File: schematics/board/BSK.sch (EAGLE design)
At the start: 58 parts, among them IC2 MAX809REUR, J1 idc_2x5, SW1 RST

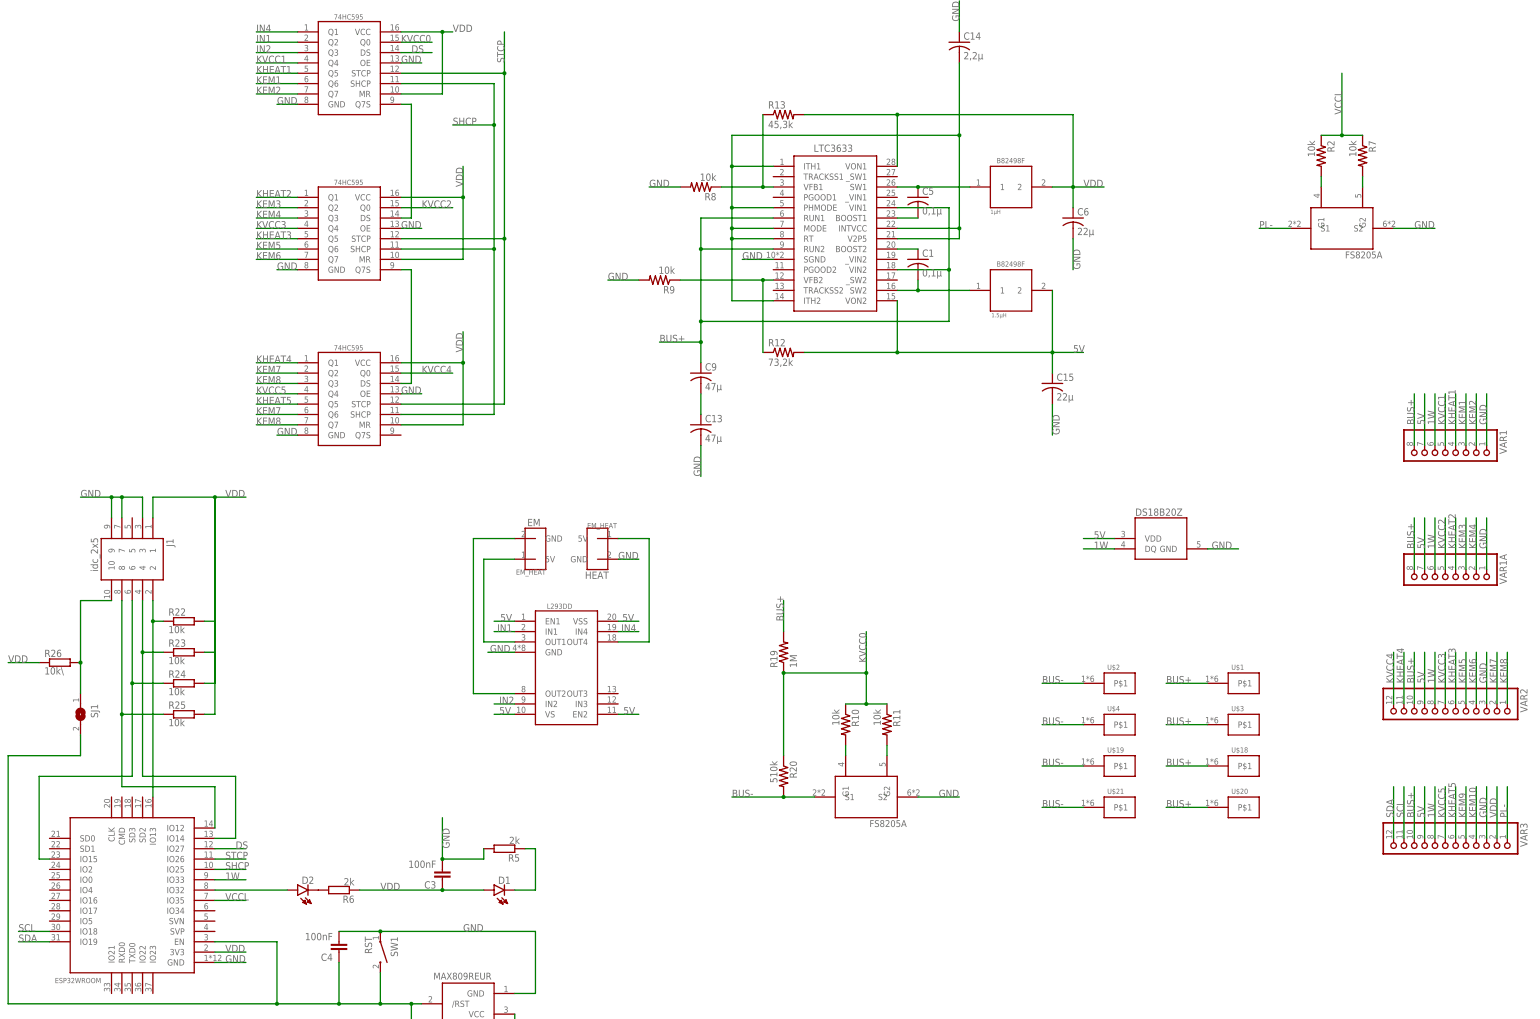
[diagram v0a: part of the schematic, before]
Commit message: изменен БСК4
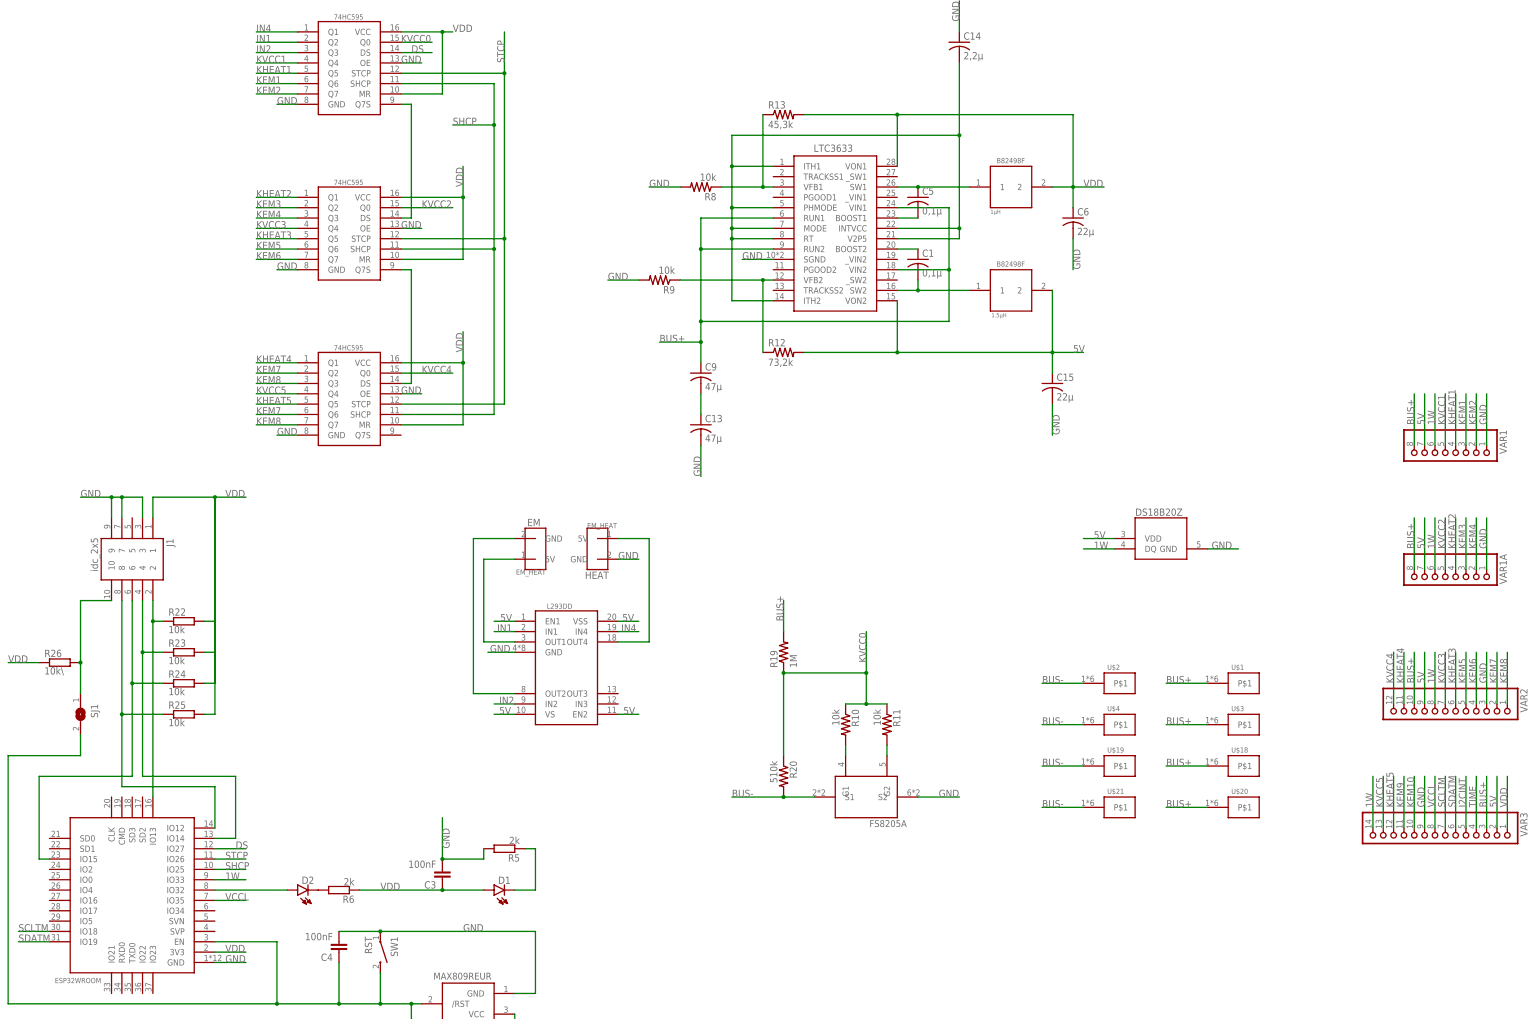
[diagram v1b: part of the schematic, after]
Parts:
- removed R2, R7: 10k, resistor:R-US_R0603
- removed U$16: FS8205A, CanCubeSat:FS8205A
- VAR3: device pinheadCS:PINHD-1X12 -> pinheadCS:PINHD-1X14
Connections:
- removed net N$4: R2.2, U$16.G1
- removed net N$6: R7.2, U$16.G2
- removed net PL-: U$16.S1, VAR3.1
- removed net SCL: U$13.IO18, VAR3.11
- removed net SDA: U$13.IO19, VAR3.12
- new net I2CINT: VAR3.5
- new net SCLTM: U$13.IO18, VAR3.7
- new net SDATM: U$13.IO19, VAR3.6
- new net TIME: VAR3.4
- net 1W: now also VAR3.14; no longer VAR3.8
- net 5V: now also VAR3.2; no longer VAR3.9
- net BUS+: now also VAR3.3; no longer VAR3.10
- net GND: now also VAR3.9; no longer U$16.S2, VAR3.3
- net KEM10: now also VAR3.10; no longer VAR3.4
- net KEM9: now also VAR3.11; no longer VAR3.5
- net KHEAT5: now also VAR3.12; no longer VAR3.6
- net KVCC5: now also VAR3.13; no longer VAR3.7
- net VCCL: now also VAR3.8; no longer R2.1, R7.1
- net VDD: now also VAR3.1; no longer VAR3.2

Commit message: изменен БСК1
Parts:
- removed C3, C4: 100nF, rcl:C-EUC0603
- removed D1, D2: HLMP6, display-hp:HLMP6
- removed IC2: MAX809REUR, MAX809_:MAX809EUR
- removed J1: idc_2x5, idc_2x5:3221-10-0100-00
- removed R21, R22, R23, R24, R25: 10k, resistor-shunt:BVS
- removed R26: 10k\, resistor-shunt:BVS
- removed R5, R6: 2k, resistor-shunt:BVS
- removed SW1: RST, 1437566-3:1437566-3
- added C2, C7: 10µ, rcl:C-USC0603
- added C33: 0,1µ, rcl:C-USC0603
- added R1: 510k, resistor:R-US_R0603
- added U$16: USB-C, CanCubeSat:USB-C
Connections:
- removed net N$17: D1.K, R5.2
- removed net N$18: D2.K, R6.1
- removed net N$21: C4.1, IC2./RST, R21.2, SJ1.2, SW1.2, U$13.EN
- removed net N$23: J1.4, R23.2, U$13.IO14
- removed net N$26: J1.8, R25.2, U$13.IO12
- removed net N$27: J1.6, R24.2, U$13.IO15
- removed net N$29: J1.10, R26.1, SJ1.1
- removed net VDD3: D2.A, U$13.IO32
- new net N$44: U$16.GND
- new net N$45: U$16.TX+
- new net N$46: U$16.VBUS
- new net N$47: U$16.RX+
- new net N$48: U$16.RES
- new net N$49: U$16.SWC
- new net N$50: U$16.SWD
- new net N$55: SJ1.2, U$13.IO0
- net GND: now also C2.2, C33.2, C7.2, SJ1.1; no longer C3.2, C4.2, IC2.GND, J1.3, J1.7, J1.9, R5.1, SW1.1
- net N$22: now also C7.1, R1.2, U$13.EN; no longer J1.2, R22.2, U$13.IO13
- net VDD: now also C2.1, C33.1, R1.1; no longer C3.1, D1.A, IC2.VCC, J1.1, R21.1, R22.1, R23.1, R24.1, R25.1, R26.2, R6.2
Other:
- moved on the sheet: SJ1

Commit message: доработана схема БСК1
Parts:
- removed SJ1: (no value), jumper:SJW
- removed U$14: FS8205A, CanCubeSat:FS8205A
- added R2: 5k, resistor:R-US_R0603
- added U$22: FS8205A+, CanCubeSat:FS8205A+
- C7: value 10µ -> 1nF
- R1: value 510k -> 12k
- U$5: value DS18B20ZDS18B20Z -> DS18B20Z; device CanCubeSat:DS18B20ZDS18B20Z -> CanCubeSat:DS18B20Z
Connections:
- removed net N$22: C7.1, R1.2, U$13.EN
- removed net N$44: U$16.GND
- removed net N$45: U$16.TX+
- removed net N$46: U$16.VBUS
- removed net N$47: U$16.RX+
- removed net N$48: U$16.RES
- removed net N$49: U$16.SWC
- removed net N$50: U$16.SWD
- removed net N$55: SJ1.2, U$13.IO0
- new net BUS+1: U$1.P$1
- new net BUS+2: U$18.P$1
- new net BUS+3: U$20.P$1
- new net BUS-1: U$4.P$1
- new net BUS-2: U$19.P$1
- new net BUS-3: U$21.P$1
- new net EN: C7.1, R1.1, U$13.EN, U$16.RES/EN
- new net HEAT: U$10.HEAT, U$13.HEAT, U$22.HEAT, U$5.HEAT, U$8.HEAT
- new net IO0: R2.1, U$13.IO0, U$16.IO0
- new net RX-C: U$13.RXD0, U$16.SWD/RXD
- new net TX-C: U$13.TXD0, U$16.SWC/TXD
- net BUS+: now also U$16.NC/VBUS; no longer U$1.P$1, U$18.P$1, U$20.P$1
- net BUS-: now also U$22.S1; no longer U$14.S1, U$19.P$1, U$21.P$1, U$4.P$1
- net GND: now also U$16.GND, U$22.S2; no longer SJ1.1, U$14.S2
- net KEM10: now also U$17.Q7
- net KEM7: no longer U$17.Q6
- net KEM8: no longer U$17.Q7
- net KEM9: now also U$17.Q6
- net N$8: now also U$22.G1; no longer U$14.G1
- net N$9: now also U$22.G2; no longer U$14.G2
- net VDD: now also R1.2, R2.2; no longer R1.1
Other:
- moved on the sheet: C1, C14, C5, C7, R1

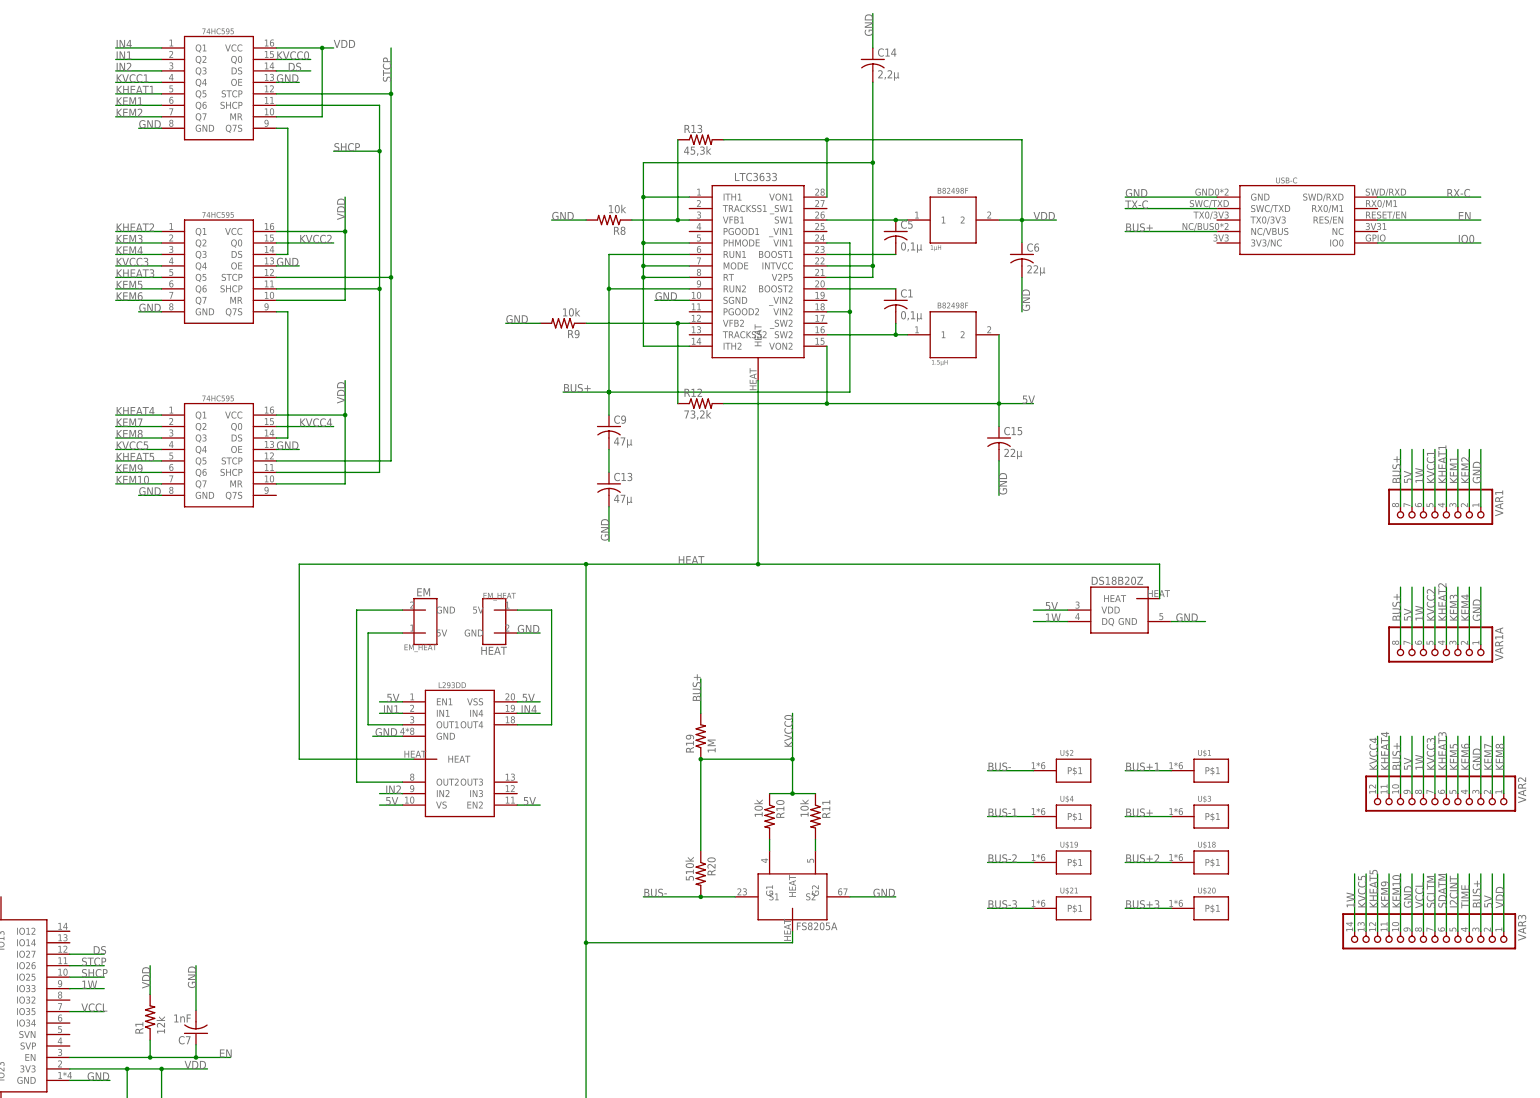
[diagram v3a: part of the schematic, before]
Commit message: Реструктурированы сигналы коммутации для плат БСК
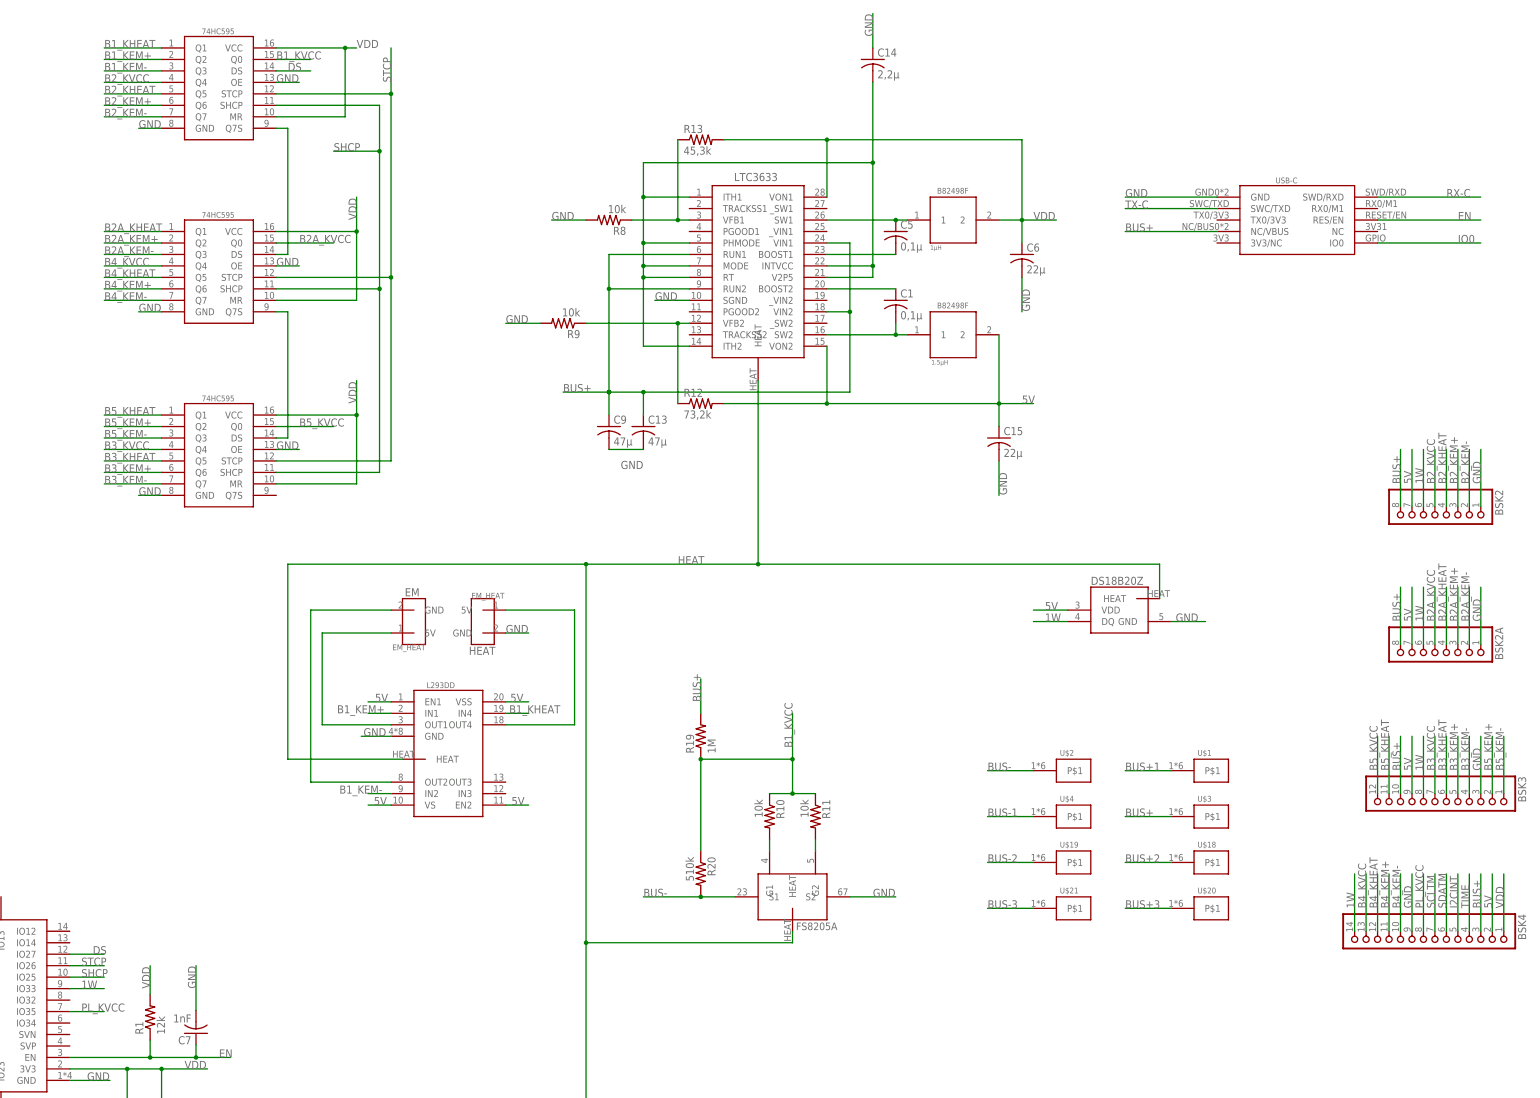
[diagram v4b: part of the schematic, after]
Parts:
- renumbered VAR1 to BSK2, VAR1A to BSK2A, VAR2 to BSK3, VAR3 to BSK4
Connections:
- net IN1 renamed B1_KEM+
- net IN2 renamed B1_KEM-
- net IN4 renamed B1_KHEAT
- net KEM1 renamed B2_KEM+
- net KEM2 renamed B2_KEM-
- net KEM3 renamed B2A_KEM+
- net KEM4 renamed B2A_KEM-
- net KEM7 renamed B5_KEM+
- net KEM8 renamed B5_KEM-
- net KHEAT1 renamed B2_KHEAT
- net KHEAT2 renamed B2A_KHEAT
- net KHEAT4 renamed B5_KHEAT
- net KVCC0 renamed B1_KVCC
- net KVCC1 renamed B2_KVCC
- net KVCC2 renamed B2A_KVCC
- net KVCC4 renamed B5_KVCC
- net VCCL renamed PL_KVCC
- removed net KEM10: BSK4.10, U$17.Q7
- removed net KEM5: BSK3.5, U$15.Q6
- removed net KEM6: BSK3.4, U$15.Q7
- removed net KEM9: BSK4.11, U$17.Q6
- removed net KHEAT3: BSK3.6, U$15.Q5
- removed net KHEAT5: BSK4.12, U$17.Q5
- removed net KVCC3: BSK3.7, U$15.Q4
- removed net KVCC5: BSK4.13, U$17.Q4
- removed net N$36: C13.1, C9.2
- new net B3_KEM+: BSK3.5, U$17.Q6
- new net B3_KEM-: BSK3.4, U$17.Q7
- new net B3_KHEAT: BSK3.6, U$17.Q5
- new net B3_KVCC: BSK3.7, U$17.Q4
- new net B4_KEM+: BSK4.11, U$15.Q6
- new net B4_KEM-: BSK4.10, U$15.Q7
- new net B4_KHEAT: BSK4.12, U$15.Q5
- new net B4_KVCC: BSK4.13, U$15.Q4
- net BUS+: now also C13.1
- net GND: now also C9.2
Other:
- moved on the sheet: C13

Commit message: доработаны схемы БСК1 и БКУ
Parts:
- added LED1: (no value), led:LEDCHIPLED_0603
- added R3: 2k, resistor:R-US_R0603
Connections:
- removed net HEAT: U$10.HEAT, U$13.HEAT, U$22.HEAT, U$5.HEAT, U$8.HEAT
- new net IO1: R3.1, U$13.IO18
- new net N$34: LED1.C, R3.2
- net 1W: now also U$13.IO21; no longer U$13.IO33
- net BUS+: now also U$16.3V3/BUS; no longer U$16.NC/VBUS
- net EN: now also U$16.NRST/EN; no longer U$16.RES/EN
- net GND: now also U$10.HEAT, U$13.HEAT, U$22.HEAT, U$5.HEAT, U$8.HEAT
- net I2CINT: now also U$13.IO5
- net IO0: now also U$16.NC/GPIO; no longer U$16.IO0
- net PL_KVCC: now also U$13.IO33; no longer U$13.IO35
- net SCLTM: now also U$13.IO16; no longer U$13.IO18
- net SDATM: now also U$13.IO17; no longer U$13.IO19
- net TIME: now also U$13.IO19
- net VDD: now also LED1.A
